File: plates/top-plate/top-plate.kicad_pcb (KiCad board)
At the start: 2 copper layers, 140.5 x 112.5 mm, 0 parts

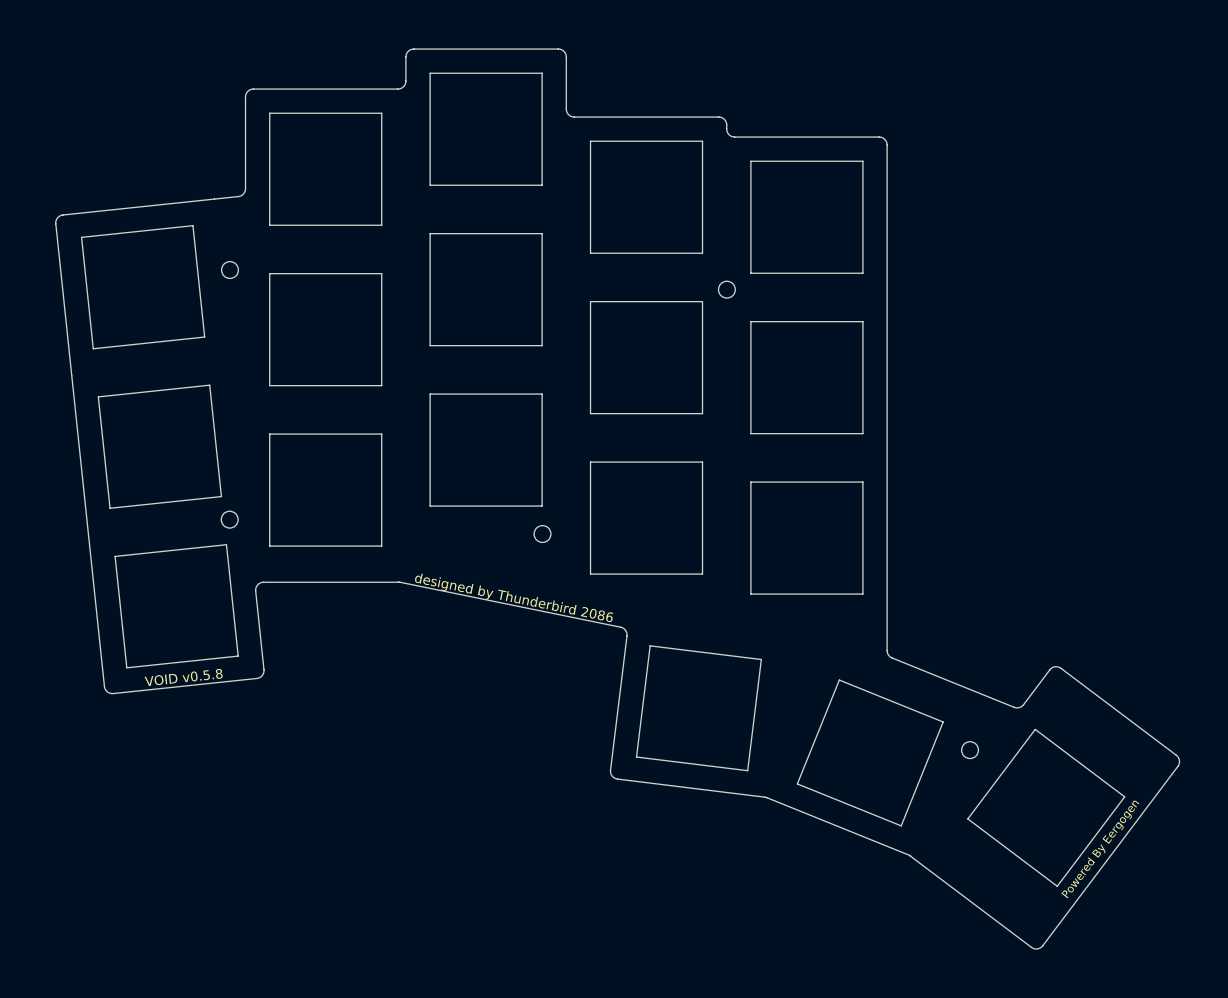
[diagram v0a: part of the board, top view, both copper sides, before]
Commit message: added choc
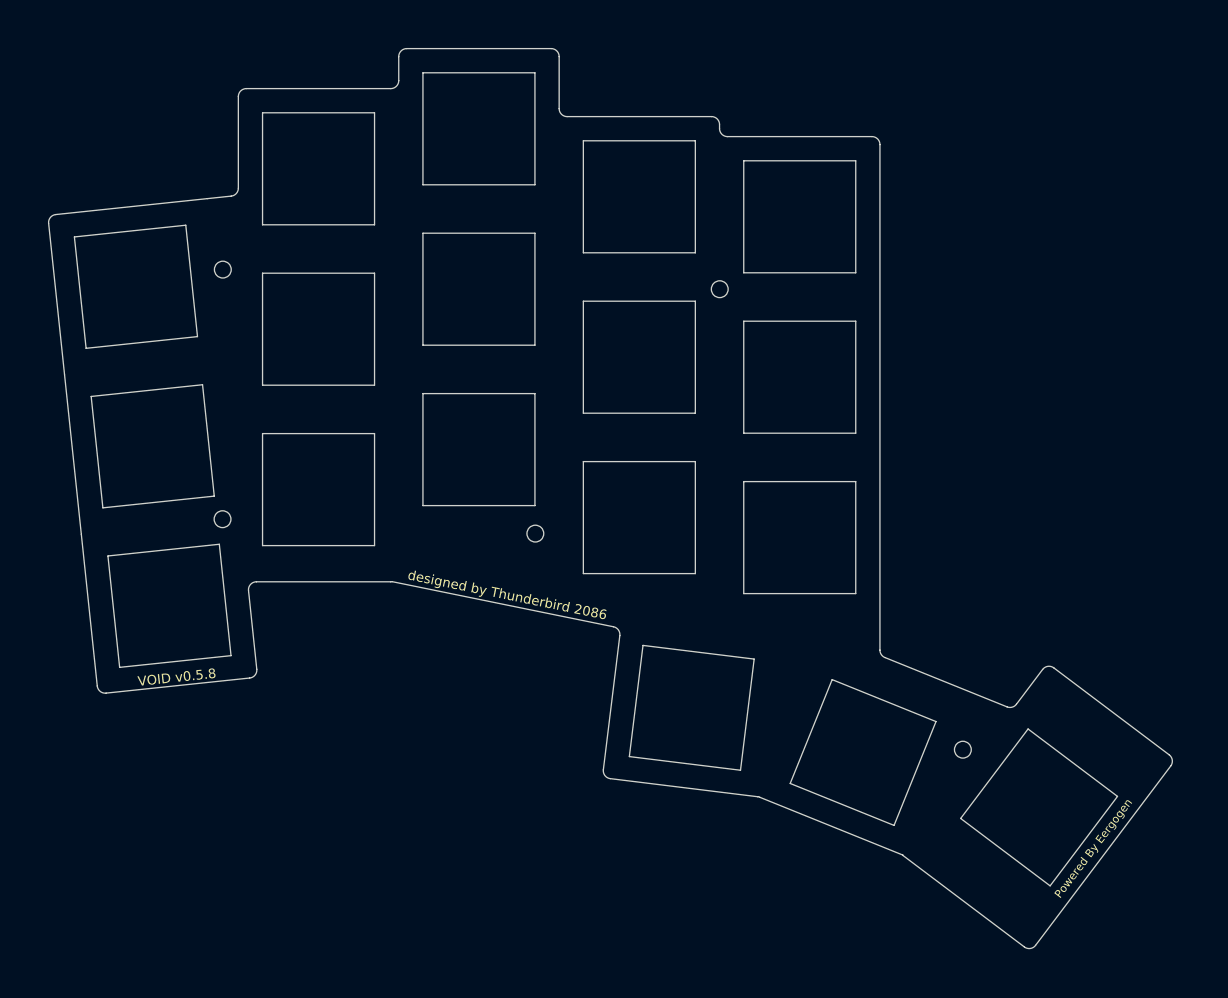
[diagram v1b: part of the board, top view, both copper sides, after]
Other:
- outline, holes or cut-outs redrawn
